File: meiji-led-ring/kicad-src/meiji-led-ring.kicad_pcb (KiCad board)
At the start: 4 copper layers, 64 x 64 mm, 69 parts, among them J1 USB_C_Receptacle_USB2.0, U1 ATSAML10D14-MFT, U2 AP5726, U3 AP5726, U4 MCP1700-3302E_SOT23

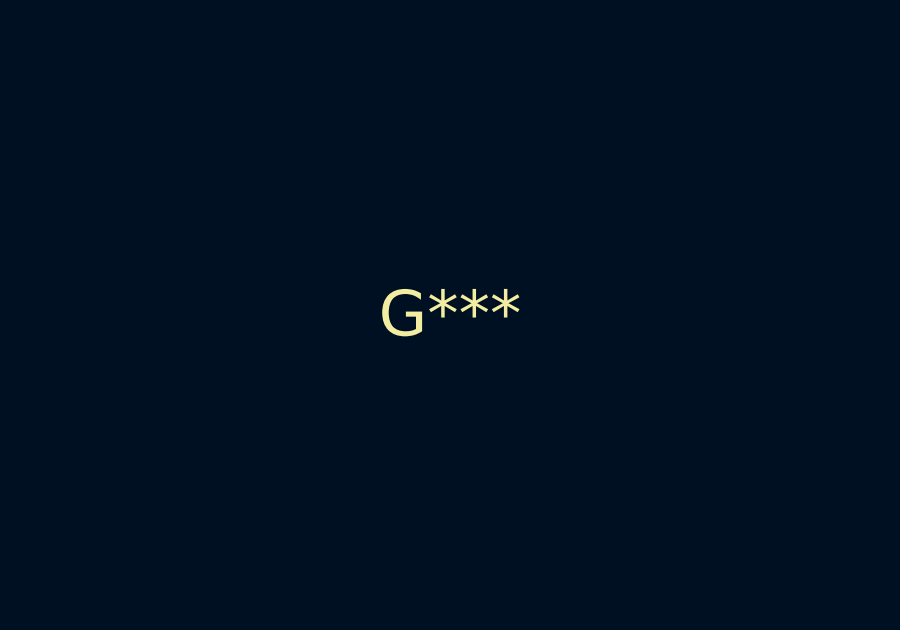
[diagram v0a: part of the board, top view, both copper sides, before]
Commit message: meji-led-ring: Add BOM values to project
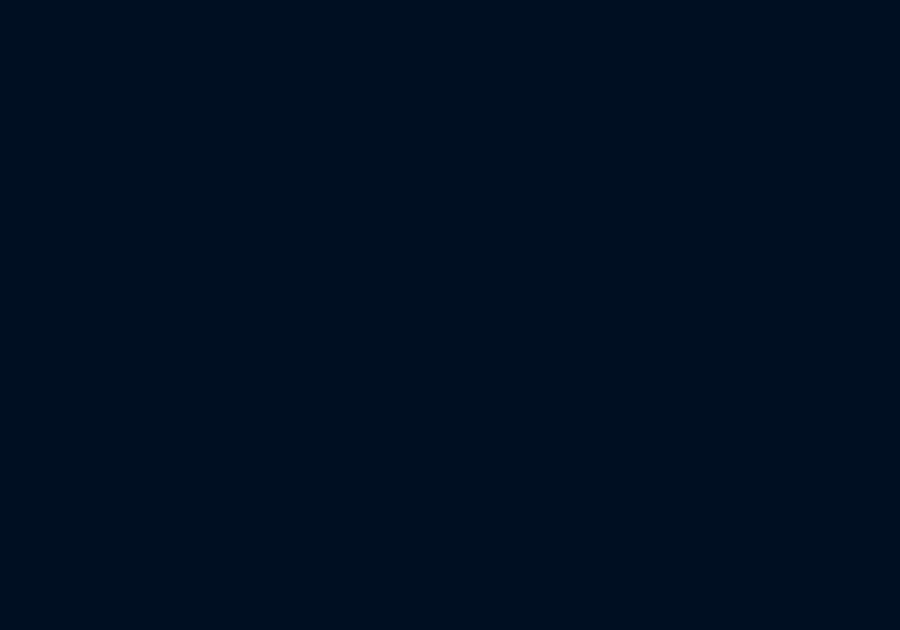
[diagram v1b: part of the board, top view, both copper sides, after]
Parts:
- R11: value 1k -> 1K
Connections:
- J1 pad A6: Net-(J1-PadA6) -> unconnected-(J1-PadA6)
- J1 pad A7: Net-(J1-PadA7) -> unconnected-(J1-PadA7)
- J1 pad A8: Net-(J1-PadA8) -> unconnected-(J1-PadA8)
- J1 pad B6: Net-(J1-PadB6) -> unconnected-(J1-PadB6)
- J1 pad B7: Net-(J1-PadB7) -> unconnected-(J1-PadB7)
- J1 pad B8: Net-(J1-PadB8) -> unconnected-(J1-PadB8)
- U1 pad 2: Net-(U1-Pad2) -> unconnected-(U1-Pad2)
- U1 pad 22: Net-(U1-Pad22) -> unconnected-(U1-Pad22)
- U1 pad 3: Net-(U1-Pad3) -> unconnected-(U1-Pad3)
- U1 pad 6: Net-(U1-Pad6) -> unconnected-(U1-Pad6)
- U1 pad 7: Net-(U1-Pad7) -> unconnected-(U1-Pad7)
